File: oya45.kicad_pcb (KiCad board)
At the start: 2 copper layers, 94 parts, among them U1 ProMicro

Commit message: added mounting holes
will have to create plate and bottom plate later. Still deciding how I should mount and what mount points/hole design I should use.
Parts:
- added H1: Hole, kbd:M2_Hole_NPTH_Outside, F.Cu at (66.7, 66.7)
- added H2: Hole, kbd:M2_Hole_NPTH_Outside, F.Cu at (219.1, 66.7)
- added H3: Hole, kbd:M2_Hole_NPTH_Outside, F.Cu at (66.7, 104.8)
- added H4: Hole, kbd:M2_Hole_NPTH_Outside, F.Cu at (219.1, 104.8)
- added H5: Hole, kbd:M2_Hole_NPTH_Outside, F.Cu at (142.9, 85.7)
- added H6: Hole, kbd:M2_Hole_NPTH_Outside, F.Cu at (104.8, 47.6)
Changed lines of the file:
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@@
     (tracks 269)
     (zones 0)
-    (modules 94)
+    (modules 100)
     (nets 70)
   )
@@
     (add_net row4)
   )
+  (module kbd:M2_Hole_NPTH_Outside (layer F.Cu)
+    (at 104.775 47.625)
+    (fp_text reference H6 (at 0 0.5) (layer F.SilkS) hide
+      (effects (font (size 1 1) (thickness 0.15)))
+    )
+    (fp_text value Hole (at 0 -0.5) (layer F.Fab)
+      (effects (font (size 1 1) (thickness 0.15)))
+    )
+    (pad "" np_thru_hole circle (at 0 0) (size 4 4) (drill 4) (layers *.Cu *.Mask))
+  )
+  (module kbd:M2_Hole_NPTH_Outside (layer F.Cu)
+    (at 142.875 85.725)
+    (fp_text reference H5 (at 0 0.5) (layer F.SilkS) hide
+      (effects (font (size 1 1) (thickness 0.15)))
+    )
+    (fp_text value Hole (at 0 -0.5) (layer F.Fab)
+      (effects (font (size 1 1) (thickness 0.15)))
+    )
+    (pad "" np_thru_hole circle (at 0 0) (size 4 4) (drill 4) (layers *.Cu *.Mask))
+  )
+  (module kbd:M2_Hole_NPTH_Outside (layer F.Cu)
+    (at 219.075 104.775)
+    (fp_text reference H4 (at 0 0.5) (layer F.SilkS) hide
+      (effects (font (size 1 1) (thickness 0.15)))
+    )
+    (fp_text value Hole (at 0 -0.5) (layer F.Fab)
+      (effects (font (size 1 1) (thickness 0.15)))
+    )
+    (pad "" np_thru_hole circle (at 0 0) (size 4 4) (drill 4) (layers *.Cu *.Mask))
+  )
+  (module kbd:M2_Hole_NPTH_Outside (layer F.Cu)
+    (at 66.675 104.775)
+    (fp_text reference H3 (at 0 0.5) (layer F.SilkS) hide
+      (effects (font (size 1 1) (thickness 0.15)))
+    )
+    (fp_text value Hole (at 0 -0.5) (layer F.Fab)
+      (effects (font (size 1 1) (thickness 0.15)))
+    )
+    (pad "" np_thru_hole circle (at 0 0) (size 4 4) (drill 4) (layers *.Cu *.Mask))
+  )
+  (module kbd:M2_Hole_NPTH_Outside (layer F.Cu)
+    (at 219.075 66.675)
+    (fp_text reference H2 (at 0 0.5) (layer F.SilkS) hide
+      (effects (font (size 1 1) (thickness 0.15)))
+    )
+    (fp_text value Hole (at 0 -0.5) (layer F.Fab)
+      (effects (font (size 1 1) (thickness 0.15)))
+    )
+    (pad "" np_thru_hole circle (at 0 0) (size 4 4) (drill 4) (layers *.Cu *.Mask))
+  )
+  (module kbd:M2_Hole_NPTH_Outside (layer F.Cu)
+    (at 66.675 66.675)
+    (fp_text reference H1 (at 0 0.5) (layer F.SilkS) hide
+      (effects (font (size 1 1) (thickness 0.15)))
+    )
+    (fp_text value Hole (at 0 -0.5) (layer F.Fab)
+      (effects (font (size 1 1) (thickness 0.15)))
+    )
+    (pad "" np_thru_hole circle (at 0 0) (size 4 4) (drill 4) (layers *.Cu *.Mask))
+  )
   (module MX_Only:MXOnly-1U-NoLED (layer B.Cu)
     (at 142.875 38.1 180)
@@
   (segment (start 226.06 109.22) (end 220.853 109.22) (width 0.254) (layer F.Cu) (net 44))
   (segment (start 76.2 41.91) (end 134.9375 41.91) (width 0.254) (layer F.Cu) (net 45))
+  (segment (start 153.67 45.085) (end 154.305 45.72) (width 0.254) (layer F.Cu) (net 45))
+  (segment (start 150.495 41.91) (end 154.305 45.72) (width 0.254) (layer B.Cu) (net 45))
+  (segment (start 134.9375 41.91) (end 150.495 41.91) (width 0.254) (layer B.Cu) (net 45))
   (segment (start 76.2 33.2105) (end 76.2 34.29) (width 0.254) (layer F.Cu) (net 46))
   (segment (start 76.0095 33.02) (end 76.2 33.2105) (width 0.254) (layer F.Cu) (net 46))
@@
   (segment (start 60.96 54.61) (end 60.96 92.71) (width 0.254) (layer B.Cu) (net 51))
   (segment (start 60.96 92.71) (end 60.96 111.76) (width 0.254) (layer B.Cu) (net 51))
-  (segment (start 89.535 45.085) (end 80.01 54.61) (width 0.254) (layer B.Cu) (net 52))
-  (segment (start 80.01 54.61) (end 80.01 111.76) (width 0.254) (layer B.Cu) (net 52))
-  (segment (start 89.535 35.56) (end 89.535 45.085) (width 0.254) (layer B.Cu) (net 52))
-  (segment (start 108.585 45.085) (end 99.06 54.61) (width 0.254) (layer B.Cu) (net 53))
-  (segment (start 108.585 35.56) (end 108.585 45.085) (width 0.254) (layer B.Cu) (net 53))
-  (segment (start 99.06 54.61) (end 99.06 111.76) (width 0.254) (layer B.Cu) (net 53))
-  (segment (start 153.67 45.085) (end 154.305 45.72) (width 0.254) (layer F.Cu) (net 45))
-  (segment (start 150.495 41.91) (end 154.305 45.72) (width 0.254) (layer B.Cu) (net 45))
-  (segment (start 134.9375 41.91) (end 150.495 41.91) (width 0.254) (layer B.Cu) (net 45))
   (segment (start 153.065725 30.48) (end 154.305 30.48) (width 0.254) (layer F.Cu) (net 51))
   (segment (start 82.249602 30.48) (end 153.065725 30.48) (width 0.254) (layer F.Cu) (net 51))
   (segment (start 77.169602 35.56) (end 82.249602 30.48) (width 0.254) (layer F.Cu) (net 51))
   (segment (start 70.485 35.56) (end 77.169602 35.56) (width 0.254) (layer F.Cu) (net 51))
+  (segment (start 89.535 45.085) (end 80.01 54.61) (width 0.254) (layer B.Cu) (net 52))
+  (segment (start 80.01 54.61) (end 80.01 111.76) (width 0.254) (layer B.Cu) (net 52))
+  (segment (start 89.535 35.56) (end 89.535 45.085) (width 0.254) (layer B.Cu) (net 52))
   (segment (start 155.968701 31.356299) (end 156.845 30.48) (width 0.254) (layer F.Cu) (net 52))
   (segment (start 155.641699 31.683301) (end 155.968701 31.356299) (width 0.254) (layer F.Cu) (net 52))
@@
   (segment (start 97.546038 35.56) (end 102.048453 31.057585) (width 0.254) (layer F.Cu) (net 52))
   (segment (start 89.535 35.56) (end 97.546038 35.56) (width 0.254) (layer F.Cu) (net 52))
+  (segment (start 108.585 45.085) (end 99.06 54.61) (width 0.254) (layer B.Cu) (net 53))
+  (segment (start 108.585 35.56) (end 108.585 45.085) (width 0.254) (layer B.Cu) (net 53))
+  (segment (start 99.06 54.61) (end 99.06 111.76) (width 0.254) (layer B.Cu) (net 53))
   (segment (start 158.508701 31.356299) (end 159.385 30.48) (width 0.254) (layer F.Cu) (net 53))
   (segment (start 153.539358 32.137311) (end 157.727689 32.137311) (width 0.254) (layer F.Cu) (net 53))

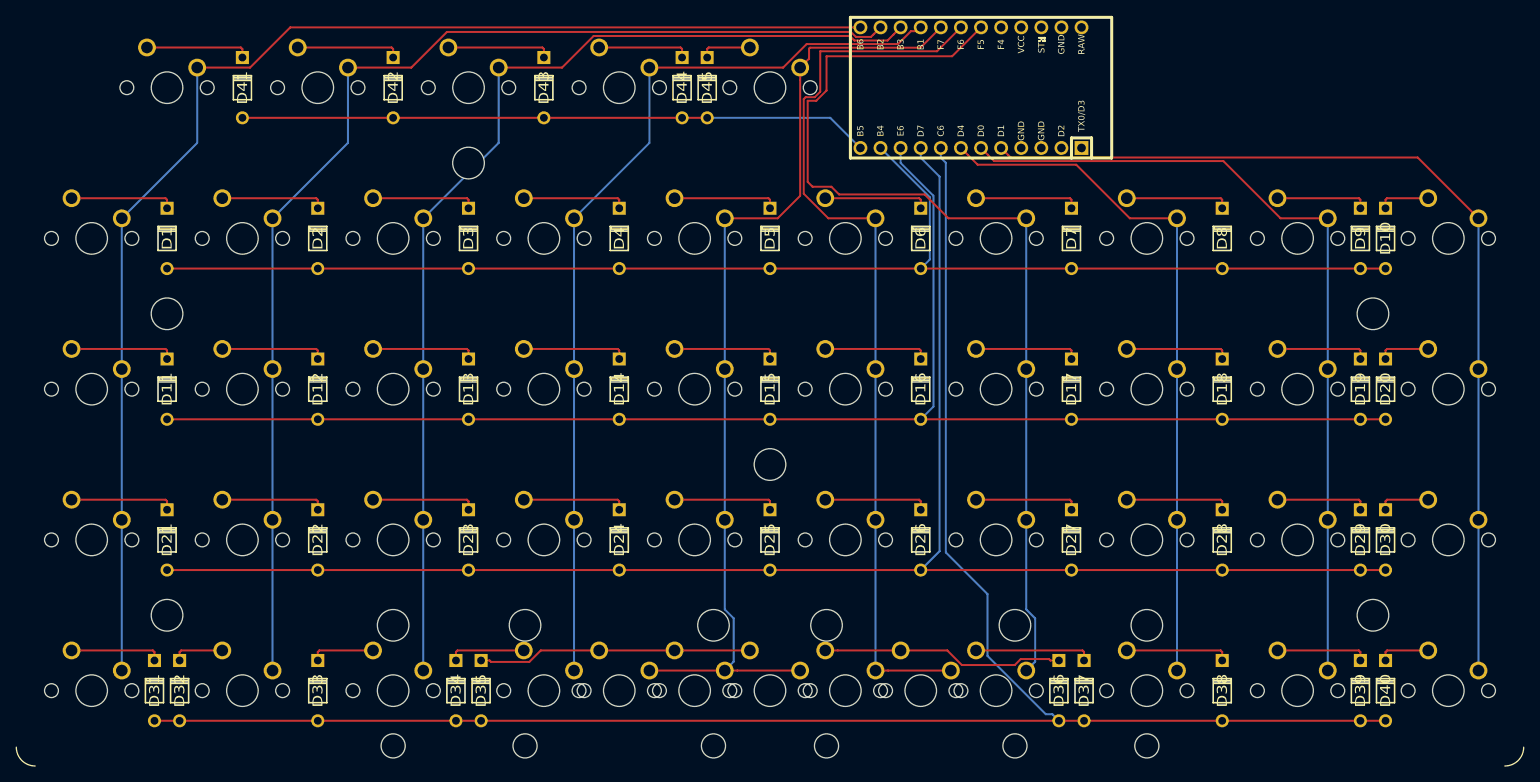
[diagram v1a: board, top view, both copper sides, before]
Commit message: diode > smd
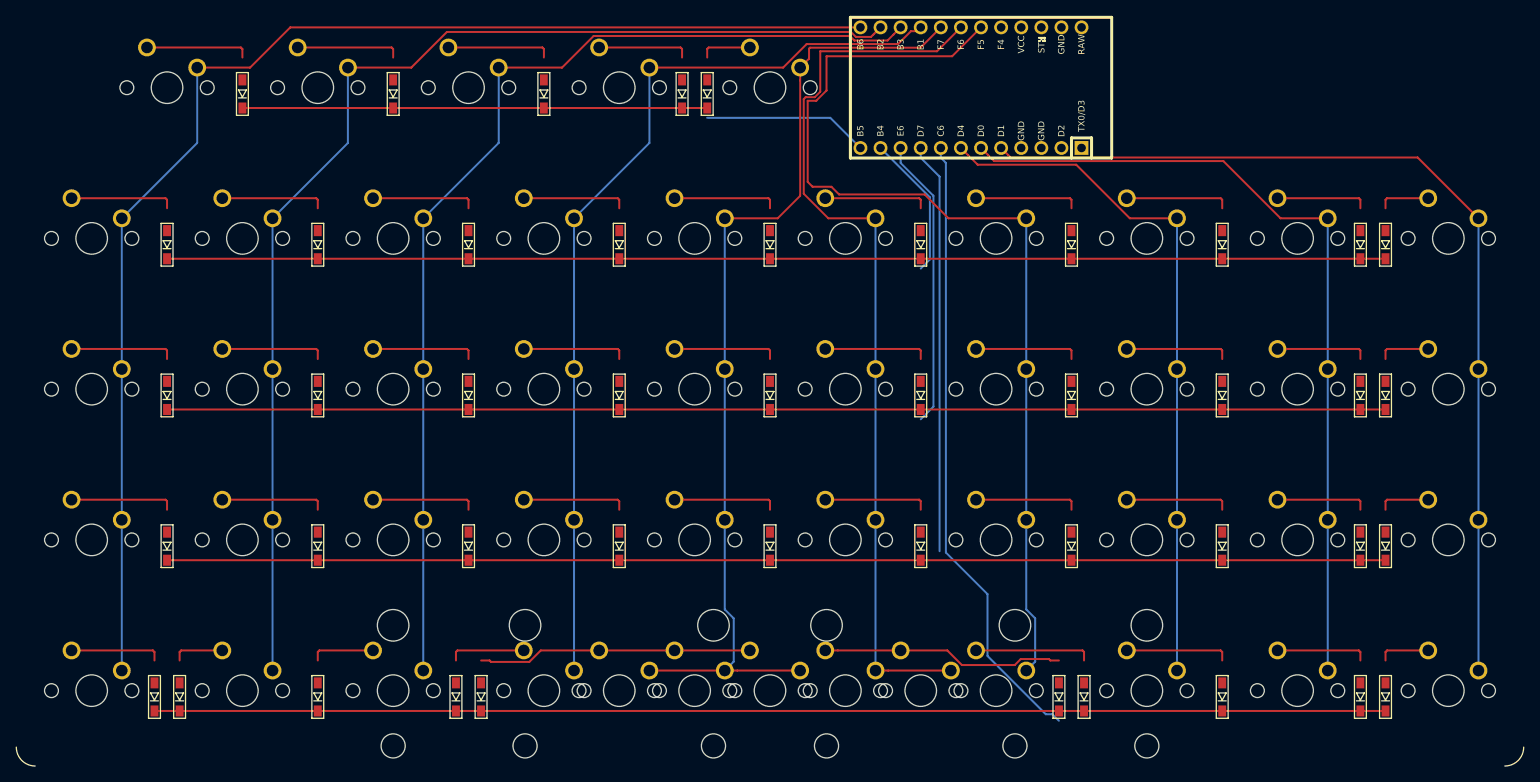
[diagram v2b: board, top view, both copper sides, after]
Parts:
- removed H1, H2, H3, H4, H5, H6: Hole, kbd:M2_Hole_NPTH_Outside
- D1, D10, D11, D12, D13, D14, D15, D16, D17, D18, D19, D2, D20, D21, D22, D23, D24, D25, D26, D27, D28, D29, D3, D30, D31, D32, D33, D34, D35, D36, D37, D38, D39, D4, D40, D41, D42, D43, D44, D45, D5, D6, D7, D8, D9: footprint Keebio-Parts:Diode -> kbd:D3_SMD_v2
- moved D1 0.79 mm to (66.7, 57.9)
- moved D10 0.79 mm to (220.7, 57.9)
- moved D11 0.79 mm to (66.7, 77.0)
- moved D12 0.79 mm to (85.7, 77.0)
- moved D13 0.79 mm to (104.8, 77.0)
- moved D14 0.79 mm to (123.8, 77.0)
- moved D15 0.79 mm to (142.9, 77.0)
- moved D16 0.79 mm to (161.9, 77.0)
- moved D17 0.79 mm to (181.0, 77.0)
- moved D18 0.79 mm to (200.0, 77.0)
- moved D19 0.79 mm to (217.5, 77.0)
- moved D2 0.79 mm to (85.7, 57.9)
- moved D20 0.79 mm to (220.7, 77.0)
- moved D21 0.79 mm to (66.7, 96.0)
- moved D22 0.79 mm to (85.7, 96.0)
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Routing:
- net row3: track 209.3 -> 205.9 mm

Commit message: much more cleaner tracing
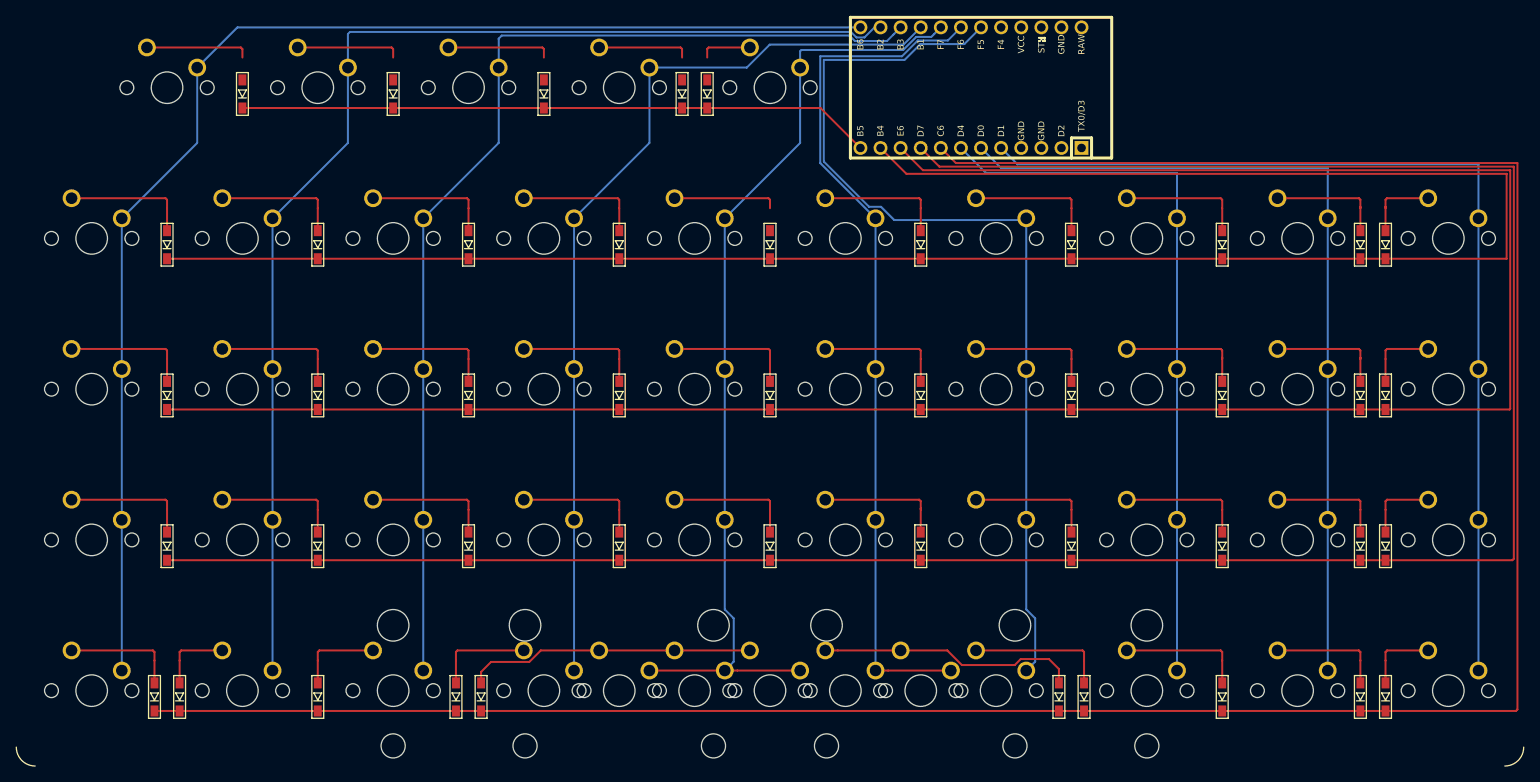
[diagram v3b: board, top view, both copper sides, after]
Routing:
- net row3: track 205.9 -> 295.8 mm
- net row1: track 172.3 -> 260.5 mm
- net row2: track 190.7 -> 278.1 mm
- net row4: track 234.6 -> 315.0 mm
- net col5: track 115.6 -> 109.3 mm
- net col6: track 126.1 -> 121.2 mm
- net col9: track 121.2 -> 125.2 mm
- net col8: track 104.6 -> 108.4 mm
- net col4: track 124.7 -> 121.2 mm
- net col7: track 88.1 -> 91.5 mm
- net Net-(D9-Pad2): track 11.6 -> 14.6 mm
- net Net-(D10-Pad2): track 6.56 -> 9.54 mm
- net Net-(D26-Pad2): track 13.2 -> 16.2 mm
- net Net-(D19-Pad2): track 11.6 -> 14.6 mm
- net Net-(D18-Pad2): track 13.2 -> 16.2 mm
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
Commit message: fixed orientation of pcb
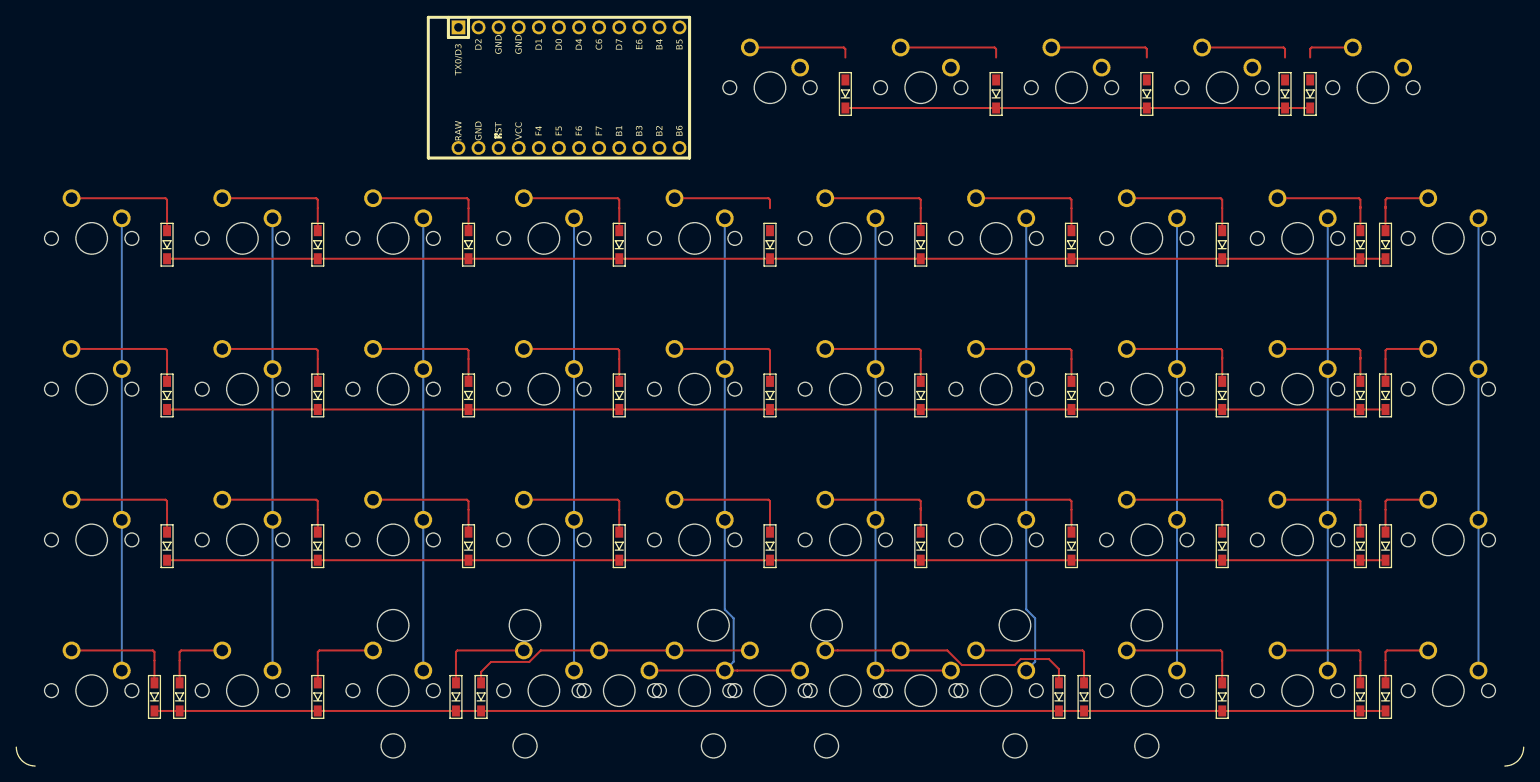
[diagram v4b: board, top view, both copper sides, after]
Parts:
- moved D44 76.2 mm to (208.0, 38.9)
- moved MX42 76.2 mm to (161.9, 38.1)
- moved D41 76.2 mm to (152.4, 38.9)
- moved D43 76.2 mm to (190.5, 38.9)
- moved MX41 76.2 mm to (142.9, 38.1)
- moved MX44 76.2 mm to (200.0, 38.1)
- moved D42 76.2 mm to (171.4, 38.9)
- moved D45 76.2 mm to (211.1, 38.9)
- moved MX43 76.2 mm to (181.0, 38.1)
- moved MX45 76.2 mm to (219.1, 38.1)
- moved U1 50.8 mm to (117.5, 38.1), turned to 0 degrees
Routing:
- net row4: track 315.0 -> 155.6 mm
- net row3: track 295.8 -> 154.0 mm
- net row2: track 278.1 -> 154.0 mm
- net col0: track 166.1 -> 57.2 mm
- net row1: track 260.5 -> 154.0 mm
- net col1: track 152.6 -> 57.2 mm
- net col2: track 135.8 -> 57.2 mm
- net col9: track 125.2 -> 57.2 mm
- net col6: track 121.2 -> 58.1 mm
- net col3: track 117.2 -> 57.2 mm
- net col8: track 108.4 -> 57.2 mm
- net col4: track 121.2 -> 77.1 mm
- net col5: track 109.3 -> 66.7 mm
- net col7: track 91.5 -> 57.2 mm
- net row0: track 80.4 -> 58.7 mm

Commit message: pcb final
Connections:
- MX41 pad 1: col0 -> col5
- MX42 pad 1: col1 -> col6
- MX43 pad 1: col2 -> col7
- MX44 pad 1: col3 -> col8
- MX45 pad 1: col4 -> col9
- U1 pad 10: row2 -> col7
- U1 pad 11: row1 -> col8
- U1 pad 12: row0 -> col9
- U1 pad 13: col0 -> col2
- U1 pad 15: col2 -> col0
- U1 pad 16: col3 -> row0
- U1 pad 17: col4 -> row1
- U1 pad 18: col5 -> row2
- U1 pad 19: col6 -> row3
- U1 pad 20: Net-(U1-Pad20) -> row4
- U1 pad 5: col9 -> Net-(U1-Pad5)
- U1 pad 6: col8 -> col3
- U1 pad 7: col7 -> col4
- U1 pad 8: row4 -> col5
- U1 pad 9: row3 -> col6
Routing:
- net row4: track 155.6 -> 307.4 mm
- net row3: track 154.0 -> 290.1 mm
- net row2: track 154.0 -> 272.2 mm
- net col9: track 57.2 -> 174.4 mm
- net row1: track 154.0 -> 255.3 mm
- net col8: track 57.2 -> 158.4 mm
- net col7: track 57.2 -> 141.9 mm
- net col6: track 58.1 -> 127.3 mm
- net col0: track 57.2 -> 126.2 mm
- net col1: track 57.2 -> 109.7 mm
- net col5: track 66.7 -> 118.4 mm
- net col3: track 57.2 -> 98.8 mm
- net col2: track 57.2 -> 93.2 mm
- net col4: track 77.1 -> 108.9 mm
- net row0: track 58.7 -> 89.4 mm
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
